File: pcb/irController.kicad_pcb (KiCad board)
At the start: 2 copper layers, 49 x 34 mm, 33 parts, among them J1 B4B-PH-K-S(LF)(SN), P1 ZX62R-B-5P, P2 GPIO_USER, Q1 Q_NMOS, SW2 SKRPACE010, U1 NJM2845, U2 ESP-13-WROOM-02, U3 IRSNS_GP1UXC41QS

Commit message: パターン引いた
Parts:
- removed the ? at (134.5, 71.5)
- removed the ? at (134.5, 100.5)
- removed P2: GPIO_USER, Socket_Strips:Socket_Strip_Straight_1x02
- removed PROG: SKRPACE010, OriginalLibSw:SKRPACE010
- added ?: MountingHole_2.2mm_M2, Mounting_Holes:MountingHole_2.2mm_M2, F.Cu at (132.5, 71.8)
- added ?: MountingHole_2.2mm_M2, Mounting_Holes:MountingHole_2.2mm_M2, F.Cu at (132.5, 100.0)
- added C5: 0.1u, Capacitor_SMD:C_0603_1608Metric, F.Cu at (134.6, 84.8)
- added IC1: ADT7410TRZ, SamacSys:SOIC127P600X175-8N, F.Cu at (139.7, 82.0)
- added JP1: SolderJumper_3_Open, Jumper:SolderJumper-3_P1.3mm_Open_RoundedPad1.0x1.5mm_NumberLabels, B.Cu at (171.2, 97.4)
- added R14: 10k, Resistor_SMD:R_0603_1608Metric, F.Cu at (138.2, 77.2)
- added R15: 10k, Resistor_SMD:R_0603_1608Metric, F.Cu at (140.0, 77.2)
- added R16: 10k, Resistor_SMD:R_0603_1608Metric, F.Cu at (132.3, 84.8)
- added R17: 10k, Resistor_SMD:R_0603_1608Metric, F.Cu at (136.4, 77.2)
- added R4: 1k, Resistor_SMD:R_0603_1608Metric, F.Cu at (157.7, 92.0)
- added SW1: SKRPACE010, OriginalLibSw:SKRPACE010, F.Cu at (156.5, 99.1)
- C1, C2: footprint Capacitors_SMD:C_1206 -> Capacitor_SMD:C_1206_3216Metric
- C3: value 0.22u -> 0.1u; footprint Capacitors_SMD:C_0603 -> Capacitor_SMD:C_0603_1608Metric
- C4: footprint Capacitors_SMD:C_0603 -> Capacitor_SMD:C_0603_1608Metric
- R4, R5: value 10k -> 1k
- moved Q1 22.8 mm to (165.5, 93.5)
- moved R4 16.4 mm to (166.6, 78.8)
- moved R6 15.6 mm to (160.0, 91.9), turned to 90 degrees
- moved R1 12.2 mm to (155.4, 91.9), turned to 270 degrees
- moved R12 8.99 mm to (167.4, 85.7), turned to 180 degrees
- moved R5 7.43 mm to (159.3, 95.2), turned to 180 degrees
- moved R11 6.97 mm to (167.4, 87.5), turned to 180 degrees
- moved R13 5.66 mm to (152.7, 95.0), turned to 0 degrees
- moved U1 5.59 mm to (134.4, 91.2), turned to 90 degrees
- moved SW2 4.86 mm to (151.6, 99.1)
- moved C1 3.09 mm to (136.7, 98.6), turned to 270 degrees
- moved C4 2.66 mm to (162.3, 92.0)
- moved R2 2.41 mm to (148.6, 91.9)
- moved ? 2.06 mm to (176.5, 100.0)
- moved ? 2.06 mm to (176.5, 72.0)
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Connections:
- net Net-(C1-Pad1) renamed +5V
- C2 pad 1: Net-(C2-Pad1) -> +3V3
- C3 pad 1: Net-(C2-Pad1) -> +3V3
- D1 pad 2: Net-(C2-Pad1) -> Net-(D1-Pad2)
- D2 pad 2: Net-(C2-Pad1) -> Net-(D1-Pad2)
- D3 pad 2: Net-(C2-Pad1) -> Net-(D1-Pad2)
- J1 pad 1: Net-(C2-Pad1) -> +3V3
- R1 pad 1: Net-(C2-Pad1) -> +3V3
- R2 pad 1: Net-(C2-Pad1) -> +3V3
- R4 pad 1: Net-(R4-Pad1) -> Net-(C4-Pad1)
- R4 pad 2: Net-(C4-Pad1) -> Net-(R4-Pad2)
- R5 pad 1: Net-(C2-Pad1) -> Net-(C4-Pad1)
- R5 pad 2: Net-(R4-Pad1) -> Net-(R5-Pad2)
- R6 pad 1: Net-(C2-Pad1) -> +3V3
- R6 pad 2: Net-(R6-Pad2) -> Net-(C4-Pad1)
- SW2 pad 1: Net-(R4-Pad1) -> Net-(R5-Pad2)
- SW2 pad 3: Net-(R4-Pad1) -> Net-(R5-Pad2)
- U1 pad VO: Net-(C2-Pad1) -> +3V3
- U2 pad 1: Net-(C2-Pad1) -> +3V3
- U2 pad 10: Net-(C4-Pad1) -> Net-(U2-Pad10)
- U2 pad 11: Net-(R12-Pad2) -> Net-(R11-Pad2)
- U2 pad 12: Net-(R11-Pad2) -> Net-(R12-Pad2)
- U2 pad 15: Net-(R6-Pad2) -> Net-(C4-Pad1)
- U2 pad 17: Net-(R6-Pad2) -> Net-(R4-Pad2)
- U2 pad 2: Net-(C2-Pad1) -> +3V3
- U3 pad 1: Net-(C2-Pad1) -> +3V3
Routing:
- net +3V3: track 0.00 -> 111.3 mm, vias 0 -> 2
- net Net-(C2-Pad1): track 109.7 -> 0.00 mm, vias 1 -> 0
- net GND: track 173.7 -> 249.8 mm, vias 14 -> 16
- net +5V: track 14.0 -> 46.7 mm, vias 0 -> 1
- net Net-(R4-Pad2): track 0.00 -> 21.6 mm
- net Net-(D1-Pad2): track 0.00 -> 18.8 mm
- net Net-(R4-Pad1): track 14.2 -> 0.00 mm, vias 2 -> 0
- net Net-(C4-Pad1): track 13.4 -> 24.9 mm
- net Net-(J1-Pad3): track 5.06 -> 16.0 mm
- net Net-(R5-Pad2): track 0.00 -> 10.7 mm, vias 0 -> 2
- net Net-(IC1-Pad1): track 4.37 -> 12.6 mm
- net Net-(J1-Pad2): track 5.12 -> 13.1 mm
- net Net-(R6-Pad2): track 7.88 -> 0.00 mm
- net Net-(IC1-Pad2): track 3.94 -> 11.3 mm
- net Net-(R11-Pad2): track 11.4 -> 4.28 mm
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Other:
- board size 49 x 34 mm -> 50 x 34 mm
- board text added: "IR Remote Controller V1.2"
- board text removed: "GPIO 13/12"
- board text removed: "IR Remote Controller V1.1"

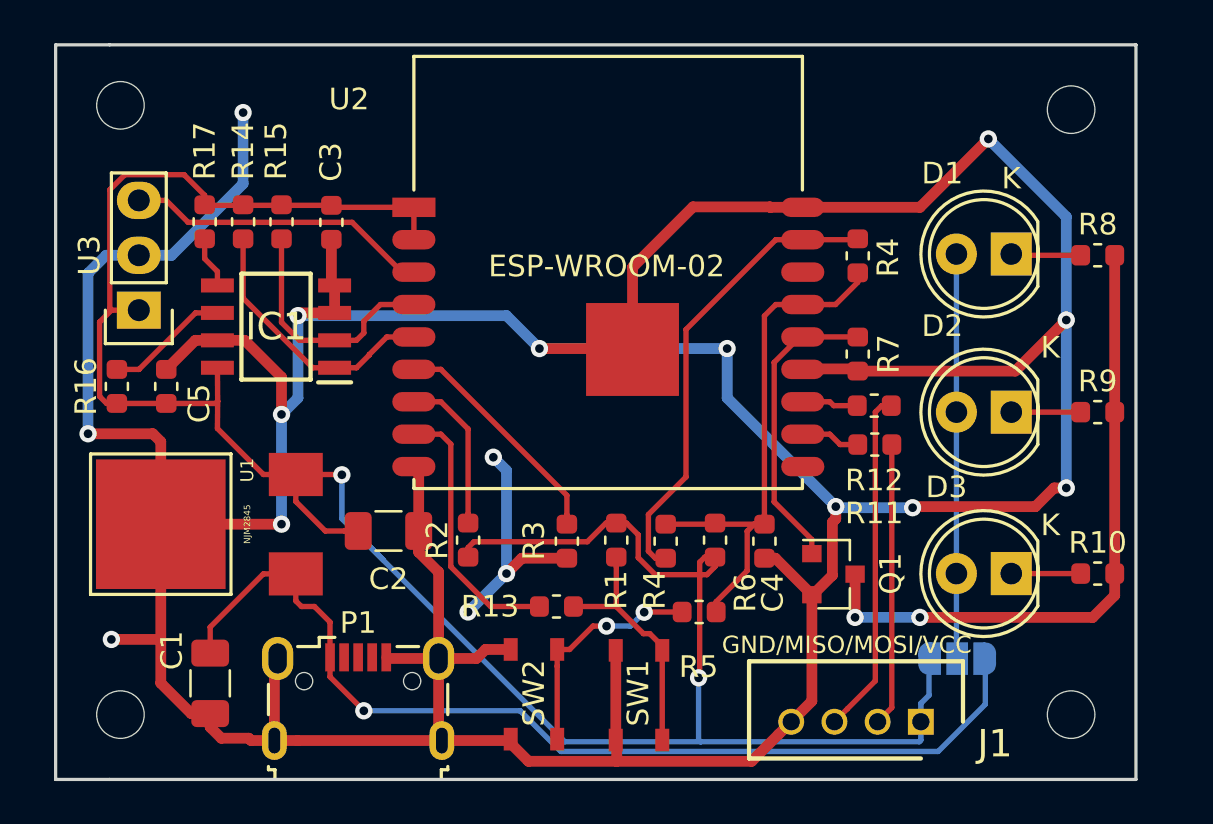
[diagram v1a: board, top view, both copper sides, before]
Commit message: LEDの駆動電流は5V固定にした
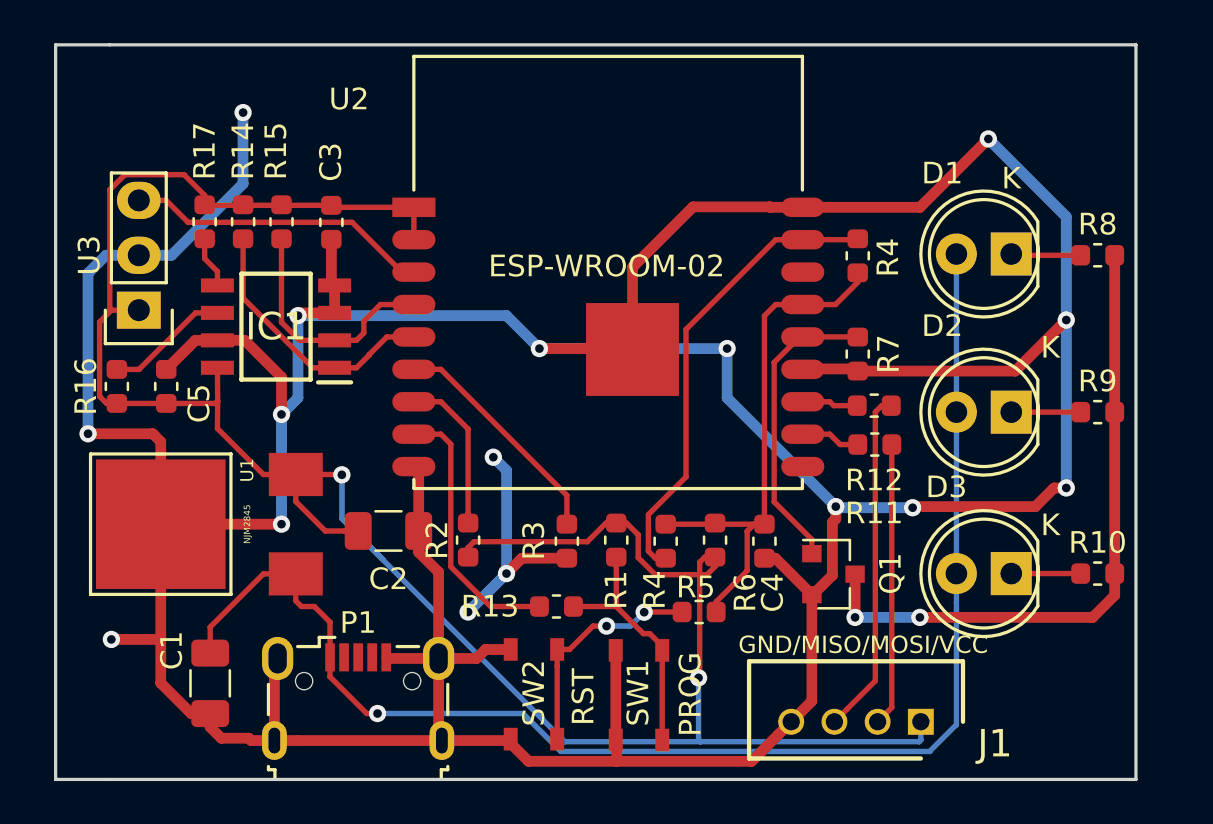
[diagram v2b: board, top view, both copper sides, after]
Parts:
- removed ? (x4): MountingHole_2.2mm_M2, Mounting_Holes:MountingHole_2.2mm_M2
- removed JP1: SolderJumper_3_Open, Jumper:SolderJumper-3_P1.3mm_Open_RoundedPad1.0x1.5mm_NumberLabels
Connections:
- D1 pad 2: Net-(D1-Pad2) -> +5V
- D2 pad 2: Net-(D1-Pad2) -> +5V
- D3 pad 2: Net-(D1-Pad2) -> +5V
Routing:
- net Net-(D1-Pad2): track 18.8 -> 0.00 mm
- net +5V: track 46.7 -> 64.7 mm
- net +3V3: track 111.3 -> 108.3 mm
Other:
- board text added: "PROG"
- board text added: "RST"

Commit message: IC発熱を考慮して再配置
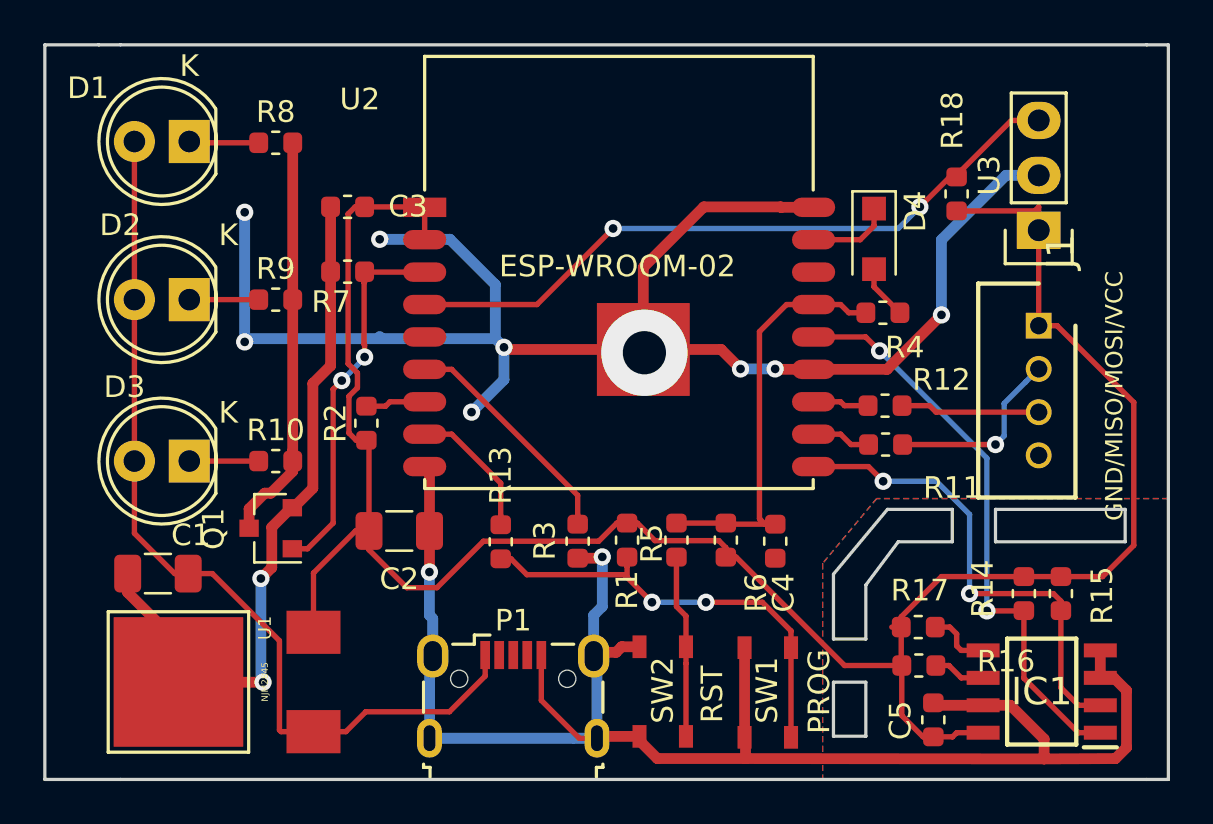
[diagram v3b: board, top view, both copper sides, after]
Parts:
- removed the R4 at (166.6, 78.8)
- removed the R4 at (157.7, 92.0)
- added D4: D, Diode_SMD:D_SOD-123F, F.Cu at (167.4, 78.0)
- added R18: 10k, Resistor_SMD:R_0603_1608Metric, F.Cu at (171.2, 75.9)
- added R4: 1k, Resistor_SMD:R_0603_1608Metric, F.Cu at (167.8, 81.4)
- moved U3 41.8 mm to (175.0, 77.6)
- moved R14 40.0 mm to (174.3, 94.4)
- moved R15 40.0 mm to (176.0, 94.4)
- moved R16 39.3 mm to (169.4, 97.7), turned to 0 degrees
- moved IC1 39.3 mm to (175.1, 98.9)
- moved C5 38.7 mm to (170.1, 100.2)
- moved D1 38.4 mm to (135.7, 73.5)
- moved D2 38.4 mm to (135.7, 80.8)
- moved D3 38.4 mm to (135.7, 88.3)
- moved R10 38.4 mm to (139.7, 88.3)
- moved R8 38.4 mm to (139.7, 73.5)
- moved R9 38.4 mm to (139.7, 80.8)
- moved R17 38.0 mm to (169.4, 95.9), turned to 0 degrees
- moved Q1 26.1 mm to (139.5, 91.4), turned to 180 degrees
- moved R7 23.9 mm to (143.0, 79.5), turned to 180 degrees
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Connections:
- P1 pad 2: Net-(P1-Pad2) -> (no net)
- P1 pad 3: Net-(P1-Pad3) -> (no net)
- P1 pad 4: Net-(P1-Pad4) -> (no net)
- U2 pad 10: Net-(U2-Pad10) -> Net-(IC1-Pad2)
- U2 pad 14: Net-(Q1-Pad1) -> Net-(IC1-Pad1)
- U2 pad 16: Net-(U2-Pad16) -> (no net)
- U2 pad 3: Net-(U2-Pad3) -> Net-(Q1-Pad1)
- U2 pad 4: Net-(IC1-Pad2) -> Net-(R18-Pad2)
- U2 pad 5: Net-(IC1-Pad1) -> (no net)
- U3 pad 3: Net-(U2-Pad3) -> Net-(R18-Pad2)
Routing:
- net GND: track 249.8 -> 188.6 mm, vias 16 -> 13
- net Net-(R18-Pad2): track 0.00 -> 32.0 mm, vias 0 -> 2
- net +5V: track 64.7 -> 42.6 mm, vias 1 -> 0
- net Net-(D4-Pad1): track 21.6 -> 3.86 mm
- net Net-(IC1-Pad1): track 12.6 -> 26.8 mm, vias 0 -> 2
- net Net-(U2-Pad3): track 14.1 -> 0.00 mm
- net Net-(Q1-Pad3): track 30.2 -> 18.8 mm, vias 2 -> 0
- net Net-(IC1-Pad2): track 11.3 -> 22.3 mm, vias 0 -> 2
- net Net-(R1-Pad2): track 11.5 -> 21.1 mm, vias 0 -> 2
- net Net-(J1-Pad3): track 16.0 -> 6.45 mm
- net +3V3: track 108.3 -> 100.3 mm, vias 2 -> 0
- net Net-(R13-Pad1): track 12.9 -> 6.88 mm
- net Net-(C4-Pad1): track 24.9 -> 19.7 mm
- net Net-(R2-Pad2): track 7.39 -> 2.78 mm
- net Net-(J1-Pad2): track 13.1 -> 8.63 mm, vias 0 -> 1
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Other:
- board size 50 x 34 mm -> 52 x 34 mm
- board text added: "IR Remote Controller V1.3"
- board text removed: "IR Remote Controller V1.2"

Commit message: tmp
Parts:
- added R19: 10k, Resistor_SMD:R_0603_1608Metric, F.Cu at (171.5, 83.0)
- added U4: DHT11, Connector_PinHeader_2.54mm:PinHeader_1x04_P2.54mm_Vertical, F.Cu at (171.5, 72.5)
- moved U3 5.90 mm to (178.0, 72.5), turned to 270 degrees
- moved R18 3.88 mm to (174.8, 77.5)
- moved J1 3.00 mm to (178.0, 82.0)
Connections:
- U2 pad 5: (no net) -> Net-(R19-Pad2)
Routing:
- net Net-(R19-Pad2): track 0.00 -> 36.0 mm, vias 0 -> 2
- net +3V3: track 100.3 -> 130.8 mm
- net GND: track 188.6 -> 200.5 mm, vias 13 -> 16
- net Net-(R18-Pad2): track 32.0 -> 42.2 mm, vias 2 -> 1
- net Net-(J1-Pad3): track 6.45 -> 9.70 mm
- net Net-(J1-Pad2): track 8.63 -> 11.6 mm
- net Net-(IC1-Pad2): track 22.3 -> 24.2 mm
- net Net-(IC1-Pad1): track 26.8 -> 27.6 mm
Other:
- outline, holes or cut-outs redrawn
- board text added: "GND/S2M/M2S/VCC"
- board text removed: "GND/MISO/MOSI/VCC"
